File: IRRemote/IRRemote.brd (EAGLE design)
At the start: 36.3 x 29.8 mm, 11 parts

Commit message: Various updates
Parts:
- U$3: value FOOTPRINTFOOTPRINT-2 -> DEVICE-PCB-TABS; device IntegerLabs:FOOTPRINT2 -> Modulo:DEVICE-PCB-TABS
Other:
- outline, holes or cut-outs redrawn
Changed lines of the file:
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@@
 <element name="U$1" library="adafruit" package="PNA460XM" value="PNA460XM" x="25.4" y="2.54" smashed="yes"/>
 <element name="U$2" library="IntegerLabs" package="SOIC14" value="TINY841" x="21.59" y="20.32" rot="R270"/>
-<element name="U$3" library="IntegerLabs" package="FOOTPRINT2" value="FOOTPRINTFOOTPRINT-2" x="0" y="0">
-<attribute name="VERSION" value="v1" x="0" y="0" size="1.778" layer="27" display="off"/>
-<attribute name="BOARD" value="IR Remote" x="0" y="0" size="1.778" layer="27" display="off"/>
-</element>
+<element name="U$3" library="Modulo" package="DEVICE-PCB-TABS" value="DEVICE-PCB-TABS" x="0" y="0"/>
 <element name="C3" library="IntegerLabs" package="0805" value=".47uF" x="16.51" y="23.1775" rot="R90"/>
 <element name="R3" library="IntegerLabs" package="0805" value="680" x="26.67" y="22.86" rot="R270"/>

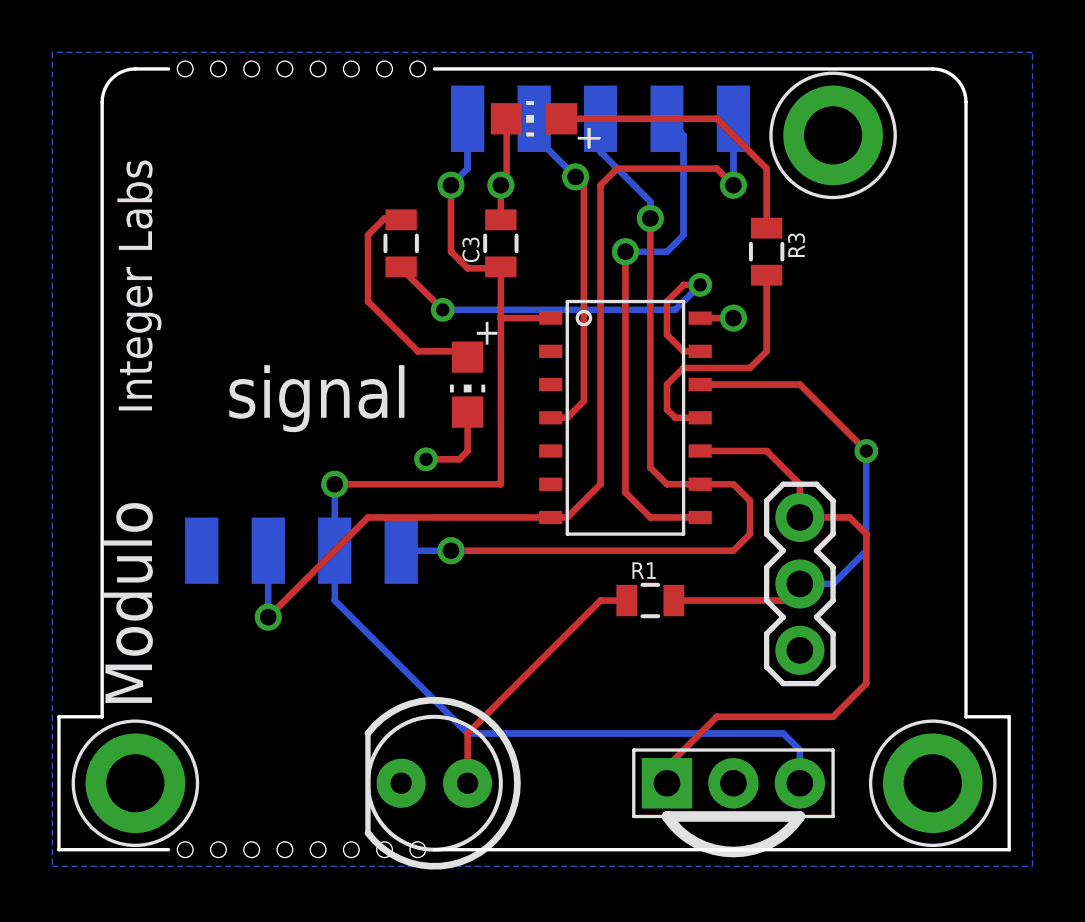
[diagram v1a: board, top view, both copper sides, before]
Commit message: Major revision of all boards. Cleaned up old files. Exported BOM csv files for all boards
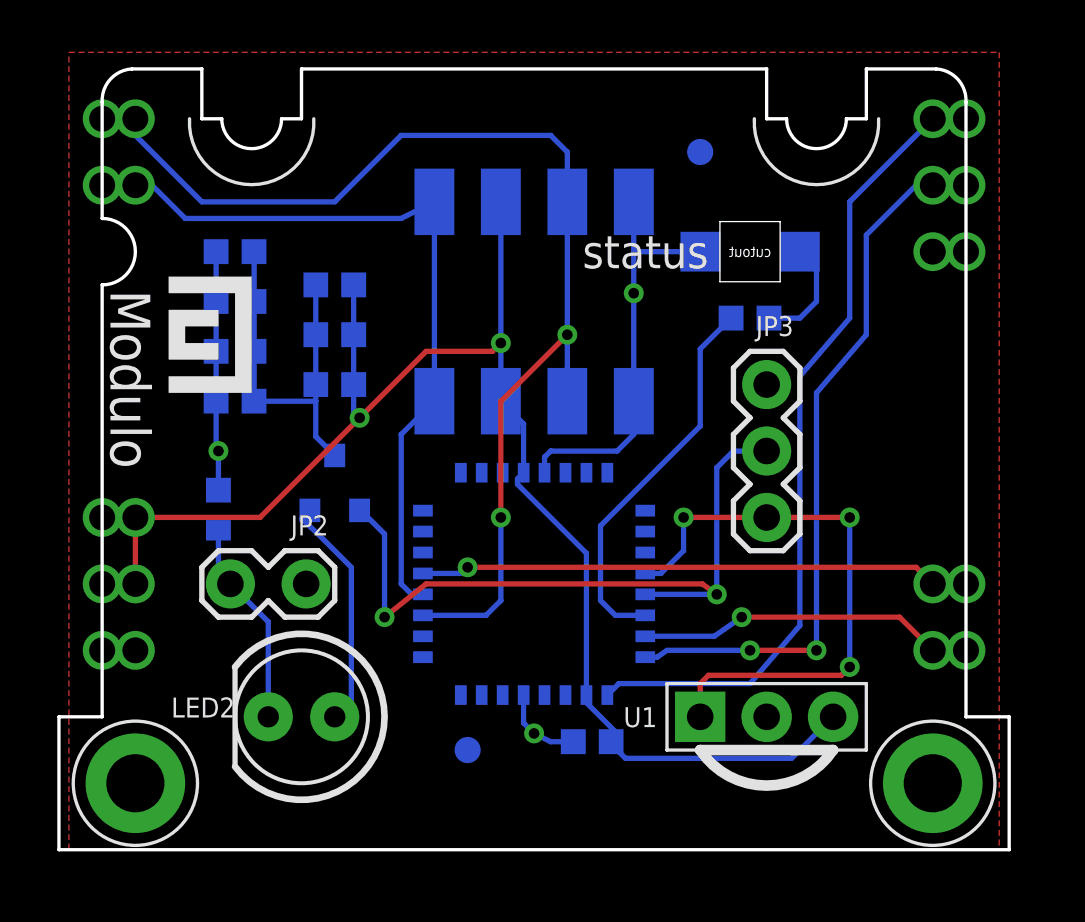
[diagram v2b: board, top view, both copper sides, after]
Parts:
- removed LED3: (no value), adafruit:CHIP-LED0805
- removed U$3: DEVICE-PCB-TABS, Modulo:DEVICE-PCB-TABS
- added C1: .1uF, Modulo:0603
- added C2, C4, C5: 10uF, Modulo:0603
- added F1, F2: FIDUCIAL, Modulo:FIDUCIAL_1MM
- added JP1: HEADER-1X4-AMPMODU, Modulo:AMPMODU-4P
- added JP3: (no value), SparkFun-Connectors:1X03
- added PCB1: DEVICE-PCB, Modulo:DEVICE-PCB
- added Q1: MOSFET-PCHANNELIRLML2244, SparkFun-DiscreteSemi:SOT23-3
- added R4: 150Ω, Modulo:0603
- added R5: 10Ω, Modulo:0603
- added U1: PNA460XM, adafruit:PNA460XM
- added U2: ATTINY48/88-TQFP, Modulo:TQFP-32
- C3: value .47uF -> 10uF; device IntegerLabs:0805 -> Modulo:0603
- JP2: value (none) -> M02LOCK; device SparkFun-Connectors:1X03 -> SparkFun-Connectors:1X02_LOCK
- LED1: value (none) -> LED-1206-REV; device adafruit:CHIP-LED0805 -> Modulo:LED-1206-REV
- R1: value 130 -> 1KΩ; device IntegerLabs:0805 -> Modulo:0603
- R2, R3: value 680 -> 150Ω; device IntegerLabs:0805 -> Modulo:0603
- U$1: value PNA460XM -> (none); device adafruit:PNA460XM -> Modulo:LOGO-SMALL
- U$2: value TINY841 -> (none); device IntegerLabs:SOIC14 -> Modulo:LOGO-SMALL
- moved U$1 27.3 mm to (4.45, 20.0), turned to 270 degrees
- moved JP2 19.2 mm to (8.89, 10.2), turned to 180 degrees
- moved R3 16.8 mm to (10.2, 19.7), flipped to the bottom, turned to 180 degrees
- moved R1 11.4 mm to (26.0, 20.3), flipped to the bottom
- moved C3 11.0 mm to (6.35, 19.1), flipped to the bottom, turned to 0 degrees
- moved LED1 9.69 mm to (26.0, 22.9), flipped to the bottom, turned to 0 degrees
- moved U$2 8.09 mm to (28.9, 16.8), flipped to the bottom, turned to 90 degrees
- moved LED2 5.68 mm to (8.89, 5.08)
- moved R2 3.00 mm to (10.2, 21.6), flipped to the bottom, turned to 180 degrees
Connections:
- removed net DATA_LED: R2.2, U$2.13
- removed net SCL/SCK: U$2.9, U$3.BUS3, U$3.PROG2
- removed net SDA/MOSI: U$2.7, U$3.BUS1, U$3.PROG4
- new net MOSI: PCB1.MOSI, U2.15
- new net N$7: LED1.A, R1.1
- new net SCK: PCB1.CLK, U2.17
- new net SCL: JP1.P$7, JP1.P$8, PCB1.SCL, U2.28
- new net SDA: JP1.P$3, JP1.P$4, PCB1.SDA, U2.27
- net GND: now also C1.2, C2.2, C4.2, C5.2, JP1.P$1, JP1.P$2, JP3.1, PCB1.GND, R5.1, U1.2, U2.21, U2.5; no longer LED2.K, LED3.C, U$1.2, U$2.14, U$3.BUS0
- net IR_LED: now also JP3.2, Q1.1, U2.13; no longer JP2.2, R1.2, U$2.12
- net IR_SENSE: now also JP3.3, U1.1, U2.12; no longer JP2.3, U$1.1, U$2.10
- net LED: now also R1.2, U2.14; no longer R3.2, U$2.11
- net MISO: now also PCB1.MISO, U2.16; no longer U$2.8, U$3.PROG3
- net N$1: now also C2.1, C3.1, C4.1, C5.1, Q1.3, R3.1, R4.1; no longer LED3.A
- net N$2: now also JP2.2, LED2.K, R5.2; no longer LED1.A, R3.1
- net N$3: now also Q1.2; no longer R1.1
- net RESET: now also PCB1.RESET, U2.29; no longer U$2.4, U$3.PROG1
- net VCC: now also C1.1, JP1.P$5, JP1.P$6, PCB1.VCC, PCB1.VPROG, R2.2, R3.2, R4.2, U1.3, U2.18, U2.4; no longer C3.1, U$1.3, U$2.1, U$3.BUS2, U$3.PROG0
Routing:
- net SDA: track 0.00 -> 44.7 mm, vias 0 -> 2
- net SDA/MOSI: track 36.9 -> 0.00 mm, vias 2 -> 0
- net SCL/SCK: track 33.3 -> 0.00 mm, vias 2 -> 0
- net SCK: track 0.00 -> 30.0 mm
- net SCL: track 0.00 -> 28.2 mm
- net GND: track 8.40 -> 28.5 mm
- net DATA_LED: track 16.9 -> 0.00 mm, vias 2 -> 0
- net MOSI: track 0.00 -> 11.7 mm, vias 0 -> 1
- net IR_LED: track 19.4 -> 27.5 mm, vias 1 -> 2
- net VCC: track 50.0 -> 57.1 mm
- net MISO: track 19.7 -> 26.5 mm, vias 1 -> 2
- net RESET: track 13.1 -> 19.9 mm
- net N$1: track 8.78 -> 14.9 mm
- net LED: track 9.60 -> 15.1 mm
- net N$7: track 0.00 -> 4.25 mm
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- added copper zone on layer 1, net GND
- removed copper zone on layer 16, net GND
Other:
- outline, holes or cut-outs redrawn
- board text added: "status"
- board text removed: "signal"

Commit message: Check point of current PCB designs. Among other things I think this change includes rewiring of programming lines on many of the boards,.
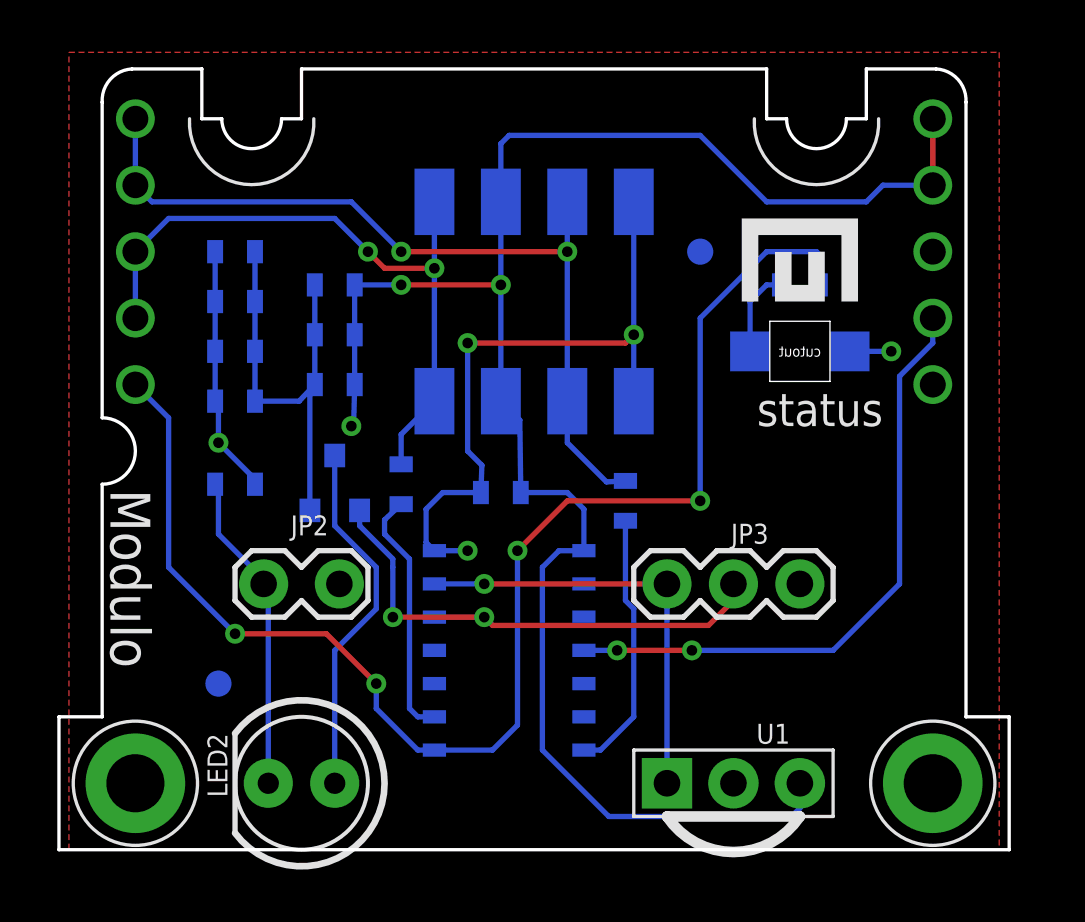
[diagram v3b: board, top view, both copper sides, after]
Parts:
- removed U2: ATTINY48/88-TQFP, Modulo:TQFP-32
- added R8, R9: 150Ω, Modulo:0603
- added U3: ATTINY841, Modulo:SOIC-14
- moved U$1 23.2 mm to (27.6, 21.6), turned to 0 degrees
- moved C1 10.1 mm to (16.5, 13.7)
- moved F1 9.86 mm to (5.71, 6.35)
- moved JP3 7.73 mm to (27.9, 10.2), turned to 180 degrees
- moved LED1 4.26 mm to (27.9, 19.1), turned to 180 degrees
- moved U$2 3.84 mm to (27.3, 13.3), turned to 0 degrees
- moved F2 3.81 mm to (24.1, 22.9)
- moved U1 2.84 mm to (25.4, 2.54)
- moved LED2 2.54 mm to (8.89, 2.54)
- moved R1 2.29 mm to (27.9, 21.6), turned to 180 degrees
- moved JP2 1.27 mm to (10.2, 10.2)
- moved R5 1.14 mm to (6.35, 14.0), turned to 0 degrees
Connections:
- removed net LED: R1.2, U2.14
- removed net MISO: PCB1.MISO, U2.16
- removed net MOSI: PCB1.MOSI, U2.15
- removed net SCK: PCB1.CLK, U2.17
- new net MISO/LED: PCB1.MISO, R1.2, U3.8
- new net SCL/SCK: R8.2, U3.9
- new net SDA/MOSI: R9.2, U3.7
- net GND: now also U3.14; no longer U2.21, U2.5
- net IR_LED: now also U3.12; no longer U2.13
- net IR_SENSE: now also U3.13; no longer U2.12
- net N$1: now also Q1.2; no longer Q1.3
- net N$3: now also Q1.3; no longer Q1.2
- net RESET: now also U3.4; no longer U2.29
- net SCL: now also PCB1.CLK, R8.1; no longer U2.28
- net SDA: now also PCB1.MOSI, R9.1; no longer U2.27
- net VCC: now also U3.1; no longer U2.18, U2.4
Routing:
- net MISO/LED: track 0.00 -> 52.9 mm, vias 0 -> 4
- net SCK: track 30.0 -> 0.00 mm
- net MISO: track 26.5 -> 0.00 mm, vias 2 -> 0
- net VCC: track 57.1 -> 72.8 mm, vias 2 -> 3
- net LED: track 15.1 -> 0.00 mm
- net SDA: track 44.7 -> 32.2 mm
- net MOSI: track 11.7 -> 0.00 mm, vias 1 -> 0
- net SDA/MOSI: track 0.00 -> 10.1 mm
- net SCL/SCK: track 0.00 -> 9.56 mm
- net GND: track 28.5 -> 36.5 mm, vias 3 -> 5
- net IR_LED: track 27.5 -> 20.7 mm
- net IR_SENSE: track 22.4 -> 16.5 mm, vias 3 -> 1
- net N$3: track 9.09 -> 13.8 mm
- net N$2: track 7.96 -> 12.2 mm
- net RESET: track 19.9 -> 23.8 mm, vias 1 -> 2
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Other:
- outline, holes or cut-outs redrawn

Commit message: Various changes
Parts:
- removed C2, C3, C4: 10uF, Modulo:0603
- removed JP2: M02LOCK, SparkFun-Connectors:1X02_LOCK
- removed Q1: MOSFET-PCHANNELIRLML2244, SparkFun-DiscreteSemi:SOT23-3
- R5: value 10Ω -> 150Ω
- R6: value 10uF -> 150Ω
- moved U$2 8.72 mm to (28.9, 21.9)
- moved R3 7.96 mm to (6.35, 12.7)
- moved R1 6.98 mm to (27.9, 14.6)
- moved R2 5.39 mm to (6.35, 17.8)
- moved R4 4.58 mm to (6.35, 20.3)
- moved R5 1.27 mm to (6.35, 15.2), turned to 180 degrees
- moved R8 1.27 mm to (11.4, 14.0)
- turned R6 to 180 degrees
- renumbered C5 to R6
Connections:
- removed net N$1: C2.1, C3.1, C4.1, Q1.2, R2.1, R3.1, R4.1, R6.1
- removed net N$2: JP2.2, LED2.K, R5.2
- removed net N$3: LED2.A, Q1.3
- new net IR_LED1: R6.2, U3.12
- new net IR_LED2: R2.2, U3.10
- new net IR_LED3: R3.2, U3.6
- new net IR_LED4: R4.2, U3.11
- new net IR_LED5: R5.2, U3.5
- net GND: now also LED2.K; no longer C2.2, C3.2, C4.2, JP2.1, R5.1, R6.2
- net IR_LED: now also LED2.A, R2.1, R3.1, R4.1, R5.1, R6.1; no longer Q1.1, U3.12
- net VCC: no longer R2.2, R3.2, R4.2
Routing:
- net IR_LED1: track 0.00 -> 22.7 mm, vias 0 -> 2
- net IR_LED: track 20.7 -> 43.0 mm, vias 2 -> 1
- net IR_LED4: track 0.00 -> 21.8 mm, vias 0 -> 2
- net IR_LED5: track 0.00 -> 20.4 mm, vias 0 -> 2
- net IR_LED2: track 0.00 -> 20.2 mm, vias 0 -> 2
- net IR_LED3: track 0.00 -> 18.5 mm, vias 0 -> 2
- net N$1: track 17.0 -> 0.00 mm
- net N$3: track 13.8 -> 0.00 mm
- net N$2: track 12.2 -> 0.00 mm
- net GND: track 36.5 -> 27.0 mm, vias 5 -> 4
- net MISO/LED: track 52.9 -> 43.8 mm, vias 4 -> 2
- net VCC: track 72.8 -> 66.5 mm, vias 3 -> 2
- net N$7: track 3.31 -> 4.89 mm
- net SCL: track 25.8 -> 26.6 mm, vias 2 -> 0
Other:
- board text removed: "status"

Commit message: Various small tweaks based on testing and feedback from manufacturer.
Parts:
- R8, R9: value 150Ω -> 0Ω
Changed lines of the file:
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@@
 <attribute name="PARTNUM" value="ATTINY841-SSUR" x="20.32" y="11.43" size="1.27" layer="28" rot="MR270" display="off"/>
 </element>
-<element name="R8" library="Modulo" package="0603" value="150Ω" x="11.43" y="13.97" rot="MR270">
-<attribute name="PARTNUM" value="ERJ-3EKF1500V" x="15.24" y="13.97" size="1.27" layer="28" rot="MR270" display="off"/>
+<element name="R8" library="Modulo" package="0603" value="0Ω" x="11.43" y="13.97" rot="MR270">
+<attribute name="PARTNUM" value="ERJ-3GEY0R00V" x="15.24" y="13.97" size="1.27" layer="28" rot="MR270" display="off"/>
 <attribute name="BOM" value="EXCLUDE" x="15.24" y="13.97" size="1.27" layer="28" rot="MR270" display="off"/>
 </element>
-<element name="R9" library="Modulo" package="0603" value="150Ω" x="21.2725" y="13.335" rot="MR270">
-<attribute name="PARTNUM" value="ERJ-3EKF1500V" x="28.8925" y="16.51" size="1.27" layer="28" rot="MR270" display="off"/>
+<element name="R9" library="Modulo" package="0603" value="0Ω" x="21.2725" y="13.335" rot="MR270">
+<attribute name="PARTNUM" value="ERJ-3GEY0R00V" x="28.8925" y="16.51" size="1.27" layer="28" rot="MR270" display="off"/>
 <attribute name="BOM" value="EXCLUDE" x="28.8925" y="16.51" size="1.27" layer="28" rot="MR270" display="off"/>
 </element>

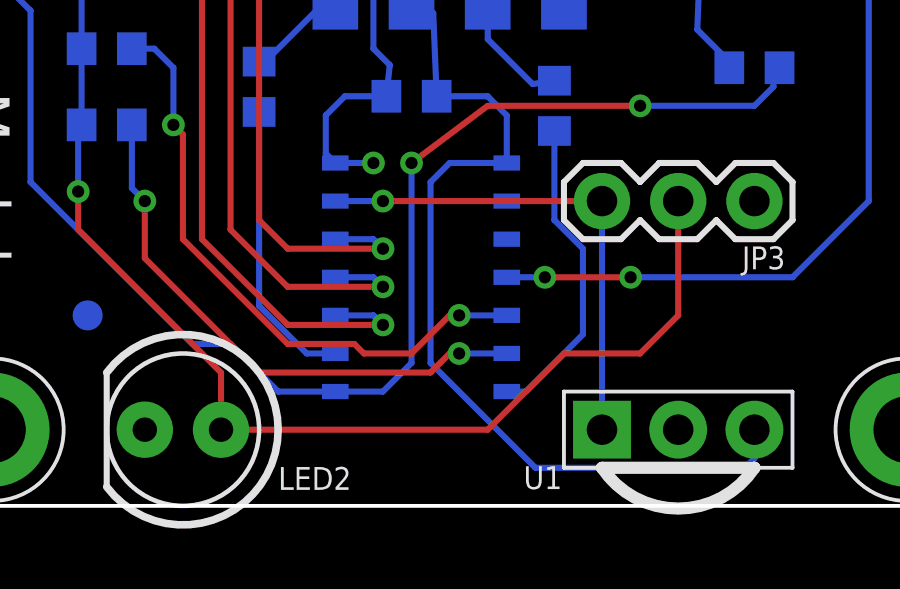
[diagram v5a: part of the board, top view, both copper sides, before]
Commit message: Various minor tweaks based on testing and feedback from manufacturer
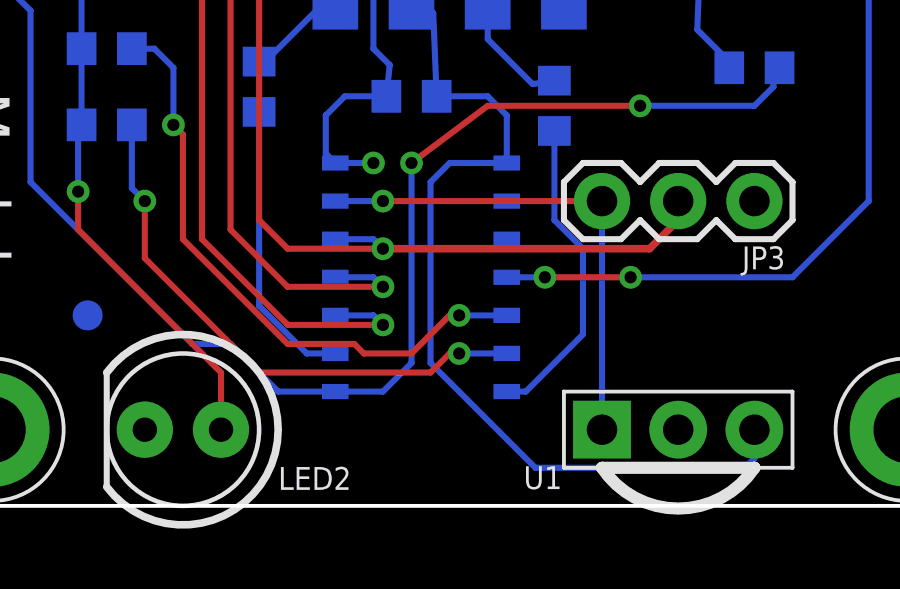
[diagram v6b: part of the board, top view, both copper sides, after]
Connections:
- net IR_LED: no longer JP3.2
- net IR_LED1: now also JP3.2
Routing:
- net IR_LED: track 43.0 -> 22.4 mm
- net IR_LED1: track 22.7 -> 33.6 mm
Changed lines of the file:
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@@
 <element name="PCB1" library="Modulo" package="DEVICE-PCB" value="DEVICE-PCB" x="0" y="0">
 <attribute name="BOARD" value="IR Remote" x="0" y="0" size="1.27" layer="27" display="off"/>
-<attribute name="VERSION" value="3" x="0" y="0" size="1.27" layer="27" display="off"/>
+<attribute name="VERSION" value="4" x="0" y="0" size="1.27" layer="27" display="off"/>
 <attribute name="PARTNUM" value="IRRemote PCB" x="0" y="0" size="1.778" layer="27" display="off"/>
 </element>
@@
 </signal>
 <signal name="IR_LED">
-<contactref element="JP3" pad="2"/>
 <contactref element="LED2" pad="A"/>
 <contactref element="R4" pad="1"/>
@@
 <wire x1="5.3975" y1="9.2075" x2="10.16" y2="4.445" width="0.2032" layer="1"/>
 <wire x1="10.16" y1="4.445" x2="10.16" y2="2.54" width="0.2032" layer="1"/>
-<wire x1="25.4" y1="10.16" x2="25.4" y2="6.35" width="0.2032" layer="1"/>
-<wire x1="25.4" y1="6.35" x2="24.13" y2="5.08" width="0.2032" layer="1"/>
-<wire x1="24.13" y1="5.08" x2="21.59" y2="5.08" width="0.2032" layer="1"/>
-<wire x1="21.59" y1="5.08" x2="19.05" y2="2.54" width="0.2032" layer="1"/>
-<wire x1="19.05" y1="2.54" x2="10.16" y2="2.54" width="0.2032" layer="1"/>
 </signal>
 <signal name="IR_SENSE">
@@
 <wire x1="7.1882" y1="22.86" x2="8.89" y2="22.86" width="0.2032" layer="16"/>
 <via x="8.89" y="22.86" extent="1-16" drill="0.4064"/>
+<contactref element="JP3" pad="2"/>
+<wire x1="25.4" y1="10.16" x2="25.4" y2="9.525" width="0.254" layer="1"/>
+<wire x1="25.4" y1="9.525" x2="24.4475" y2="8.5725" width="0.254" layer="1"/>
+<wire x1="24.4475" y1="8.5725" x2="15.5575" y2="8.5725" width="0.254" layer="1"/>
 </signal>
 <signal name="IR_LED5">

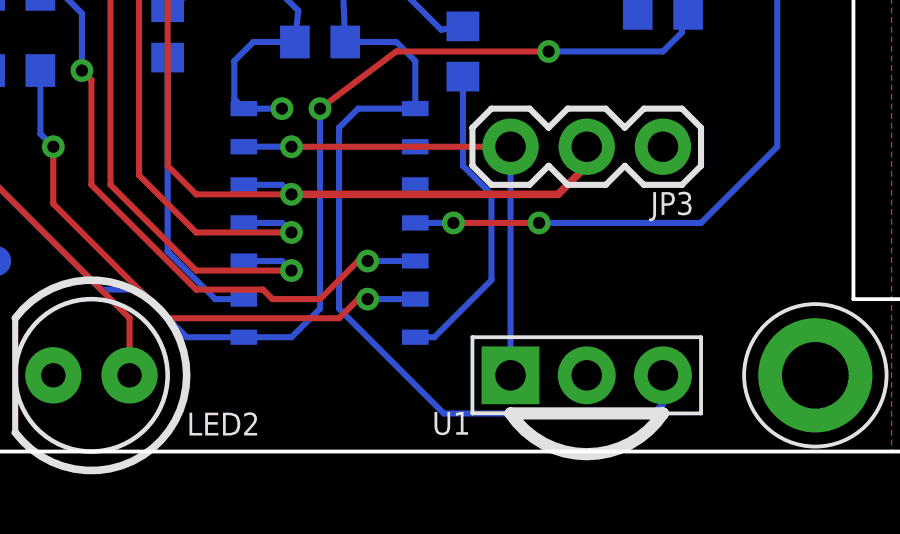
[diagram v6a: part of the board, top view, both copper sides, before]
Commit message: Added unique board prefixes to part numbers due to CM requirements
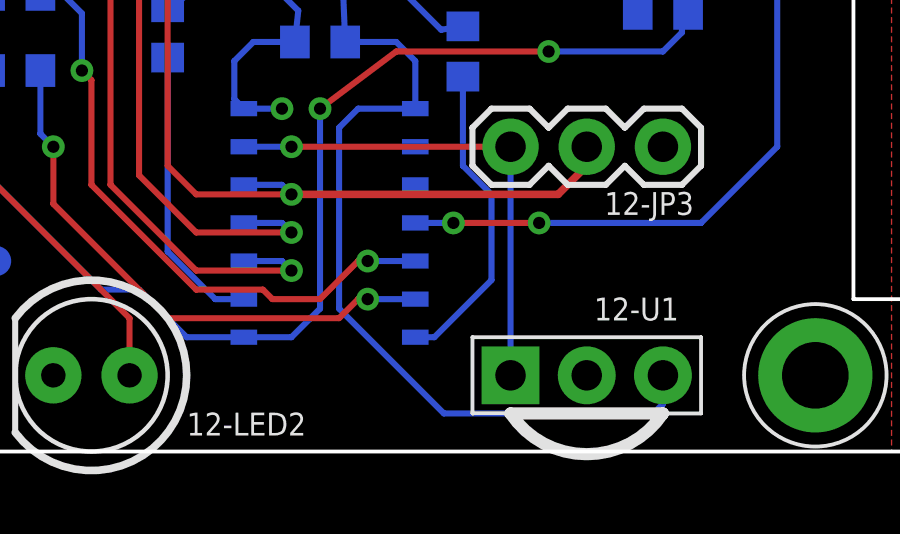
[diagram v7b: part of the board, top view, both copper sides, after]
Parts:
- renumbered C1 to 12-C1, F1 to 12-F1, F2 to 12-F2, JP1 to 12-JP1, JP3 to 12-JP3, LED1 to 12-LED1, LED2 to 12-LED2, PCB1 to 12-PCB1, R1 to 12-R1, R2 to 12-R2, R3 to 12-R3, R4 to 12-R4, R5 to 12-R5, R6 to 12-R6, R8 to 12-R8, R9 to 12-R9, U1 to 12-U1, U3 to 12-U3
